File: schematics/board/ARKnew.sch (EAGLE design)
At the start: 80 parts, among them IC2 STM32F103C8T

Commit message: Схема АРКа + устройства для него
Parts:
- removed S1: (no value), cansat-lib:UNICS-SWITCH
- removed U$3, U$4, U$5: 32961, CanCubeSat:32961
- added JP4: (no value), pinheadCS:PINHD-1X2
- added R2: 3313J-1-205E, CanCubeSat:3313J-1-205E
- added R4, R5, R6: 3314G-1-504E, CanCubeSat:3314G-1-504E
- U$1: value 32961 -> MF-R400; device CanCubeSat:32961 -> CanCubeSat:MF-R400
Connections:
- new net GND-OUT: JP1.11, JP1.12, JP2.2, JP3.2, U$1.P$2, U$12.3, U$12.5, U$12.7, U$12.9
- net 1.65: now also R4.WIPER, R5.CW; no longer U$4.WIP, U$5.CCW
- net 302: now also R5.WIPER; no longer U$5.WIP
- net 3V3: now also R4.CCW; no longer U$4.CW
- net A: now also R5.CCW; no longer U$5.CW
- net BUS+: now also JP4.2; no longer S1.P
- net BUSPLUS: now also JP4.1; no longer S1.O
- net GND: now also R2.CW, R4.CW, R6.CW, U$1.P$1; no longer JP1.11, JP1.12, JP2.2, JP3.2, U$1.CCW, U$12.3, U$12.5, U$12.7, U$12.9, U$3.CCW, U$4.CCW
- net INA_BMS+: now also R6.CCW; no longer U$1.CW
- net INA_BUS+: now also R2.CCW; no longer U$3.CW
- net N$89: now also R6.WIPER; no longer U$1.WIP
- net RUN: now also R2.WIPER; no longer U$3.WIP

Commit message: Доработана схема АРКа
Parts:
- INVERT: value INVERTER -> INVERTER.; device CanCubeSat:INVERTER -> CanCubeSat:INVERTER.

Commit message: Начато исправление разъемов
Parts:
- removed R25, R26: 5k1, resistor:R-US_R0603
- JP1: device pinheadCS:PINHD-2X8 -> pinheadCS:PINHD-2X9
- renumbered JP2 to CAM1, JP3 to CAM2, JP4 to SWITCH
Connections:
- new net AB-GND: JP1.11, JP1.12
- net 3V3: no longer R25.1, R26.1
- net BMS+: now also JP1.8
- net BUSPLUS: now also JP1.18; no longer JP1.8
- net GND-OUT: now also JP1.13, JP1.14; no longer JP1.11, JP1.12
- net SCLTM: now also JP1.15; no longer JP1.13, R25.2
- net SDATM: now also JP1.16; no longer JP1.14, R26.2
- net TIME: now also JP1.17; no longer JP1.15

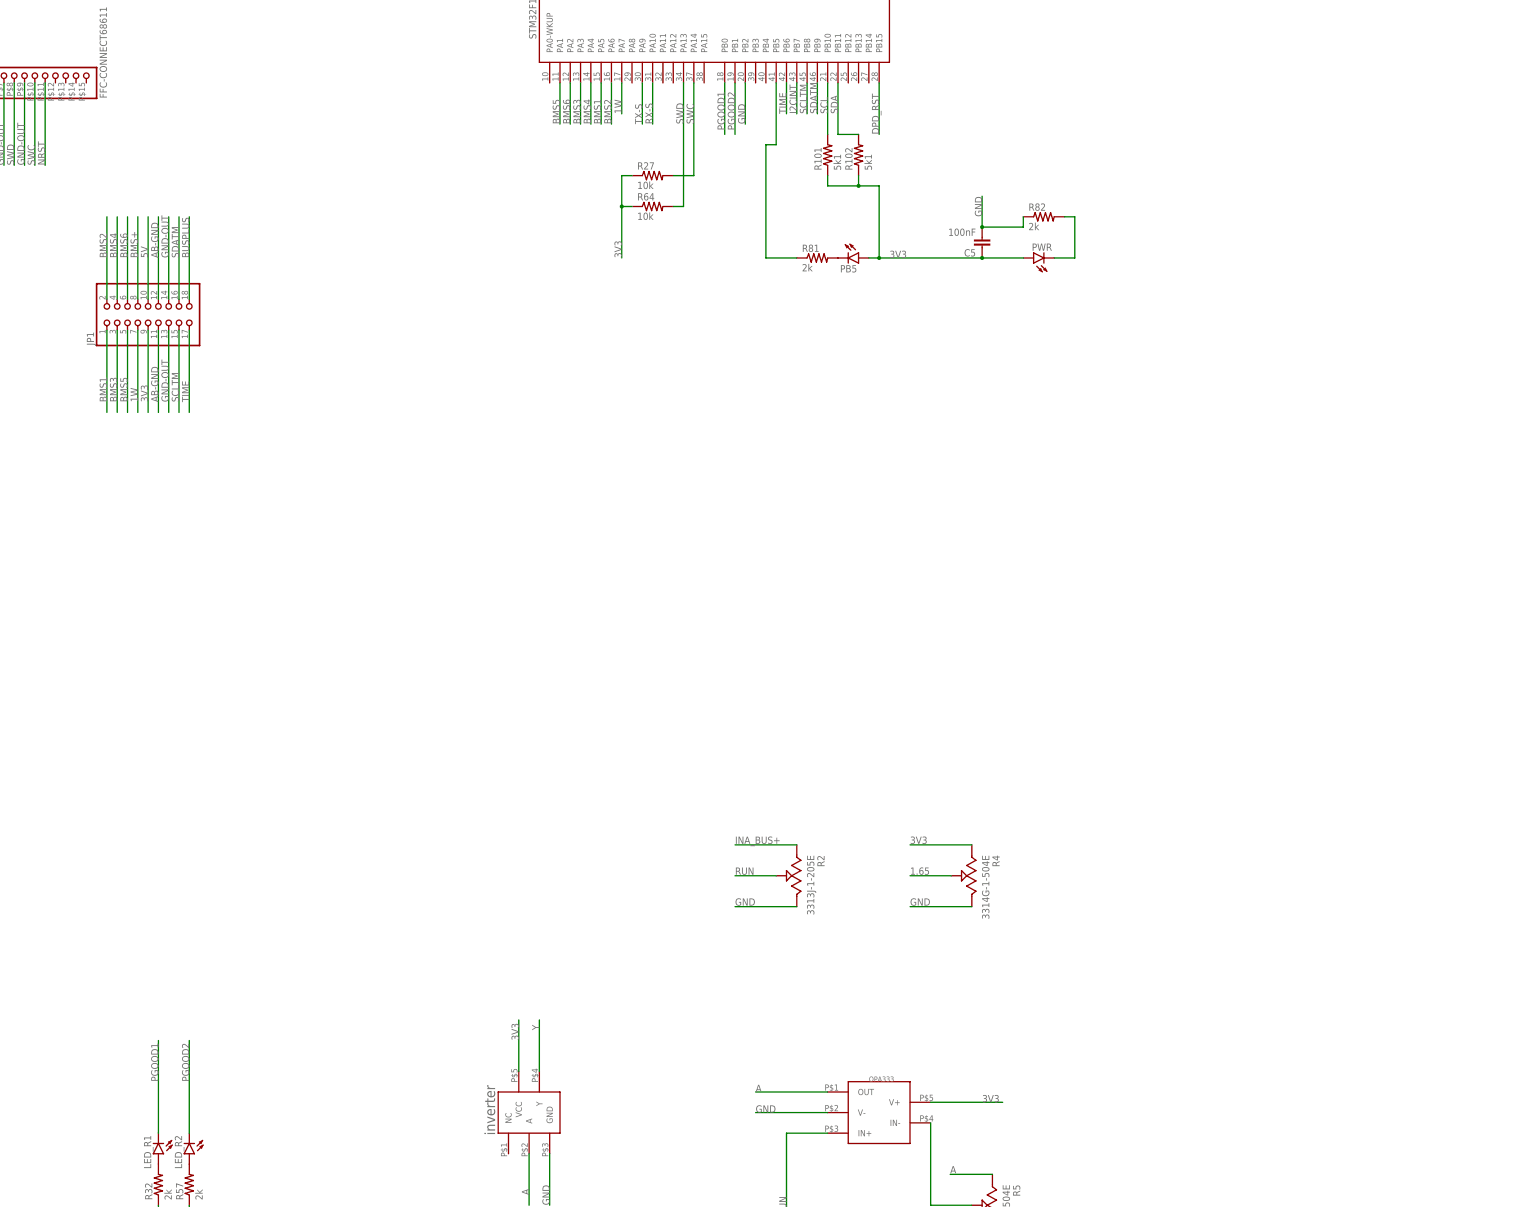
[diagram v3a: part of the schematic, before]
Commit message: Разведен АРК
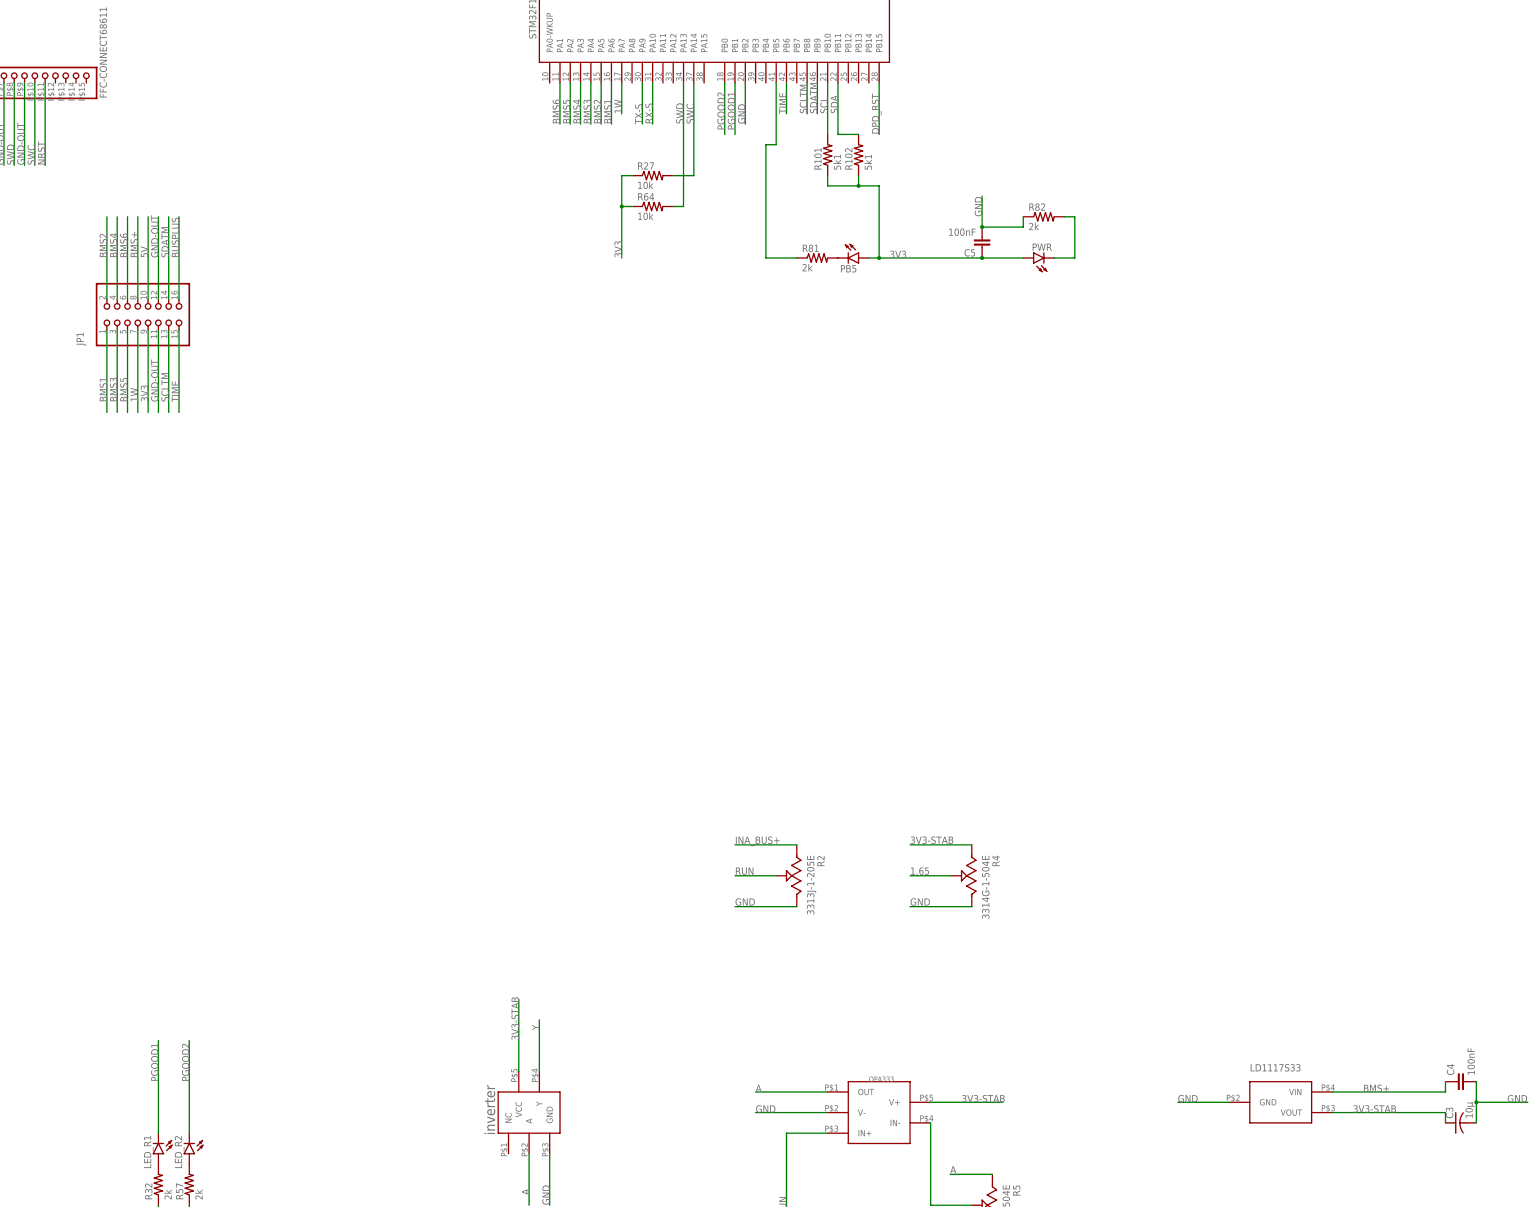
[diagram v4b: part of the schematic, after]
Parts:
- added C3: 10µ, rcl:C-USC1206
- added C4: 100nF, rcl:C-EUC0603
- added LD1117S33: LD1117S33, CanCubeSat:LD1117S33
- JP1: device pinheadCS:PINHD-2X9 -> pinheadCS:PINHD-2X8
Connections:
- removed net AB-GND: JP1.11, JP1.12
- removed net I2CINT: IC2.PB7
- new net 3V3-STAB: C3.1, INVERT.VCC, LD1117S33.VOUT, OPA.V+, R4.CCW
- net 3V3: no longer INVERT.VCC, OPA.V+, R4.CCW
- net BMS+: now also C4.1, LD1117S33.VIN
- net BMS1: now also IC2.PA6; no longer IC2.PA5
- net BMS2: now also IC2.PA5; no longer IC2.PA6
- net BMS3: now also IC2.PA4; no longer IC2.PA3
- net BMS4: now also IC2.PA3; no longer IC2.PA4
- net BMS5: now also IC2.PA2; no longer IC2.PA1
- net BMS6: now also IC2.PA1; no longer IC2.PA2
- net BUSPLUS: now also JP1.16; no longer JP1.18
- net GND: now also C3.2, C4.2, LD1117S33.GND
- net GND-OUT: now also JP1.11, JP1.12; no longer JP1.13, JP1.14
- net PGOOD1: now also IC2.PB1; no longer IC2.PB0
- net PGOOD2: now also IC2.PB0; no longer IC2.PB1
- net SCLTM: now also JP1.13; no longer JP1.15
- net SDATM: now also JP1.14; no longer JP1.16
- net TIME: now also JP1.15; no longer JP1.17
